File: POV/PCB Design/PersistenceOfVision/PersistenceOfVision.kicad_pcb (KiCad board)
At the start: 2 copper layers, 8 parts, among them SW1 SW_Push, U1 ATtiny85-20PU

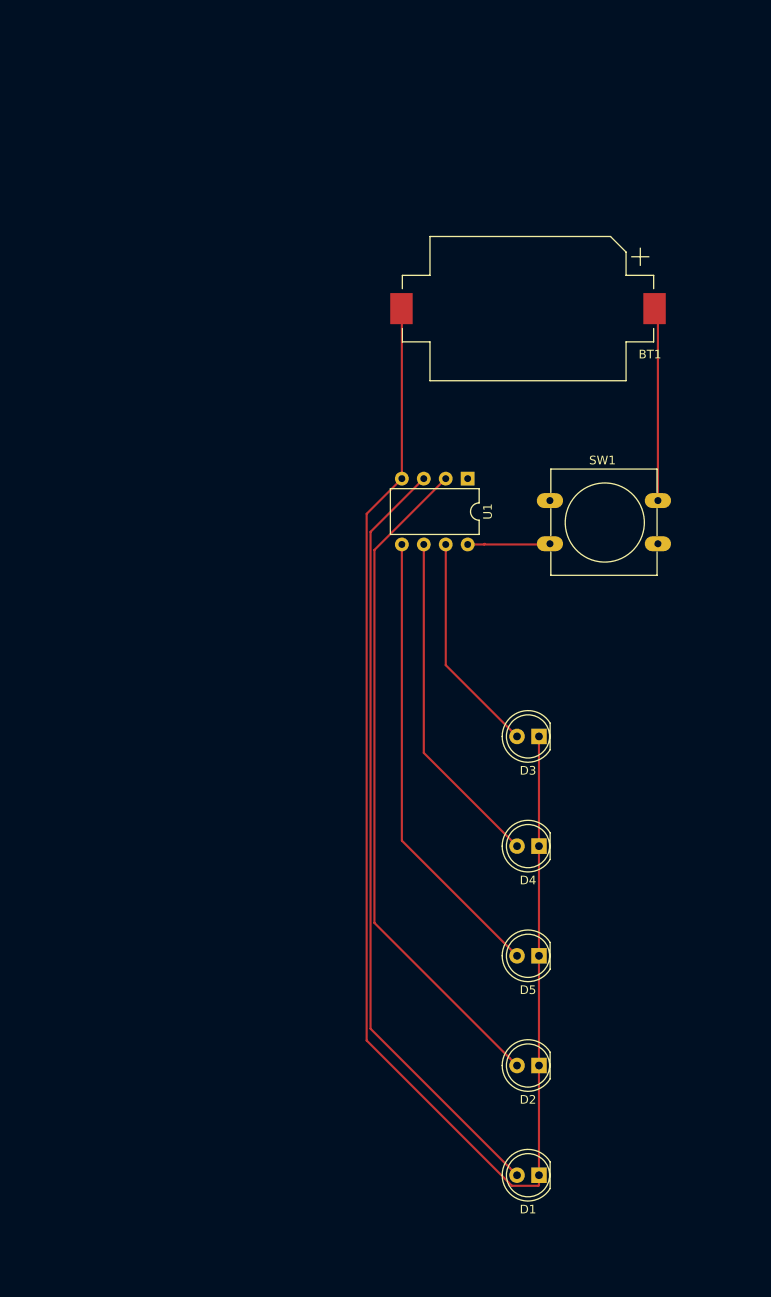
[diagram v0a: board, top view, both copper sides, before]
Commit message: Added graphics to the board
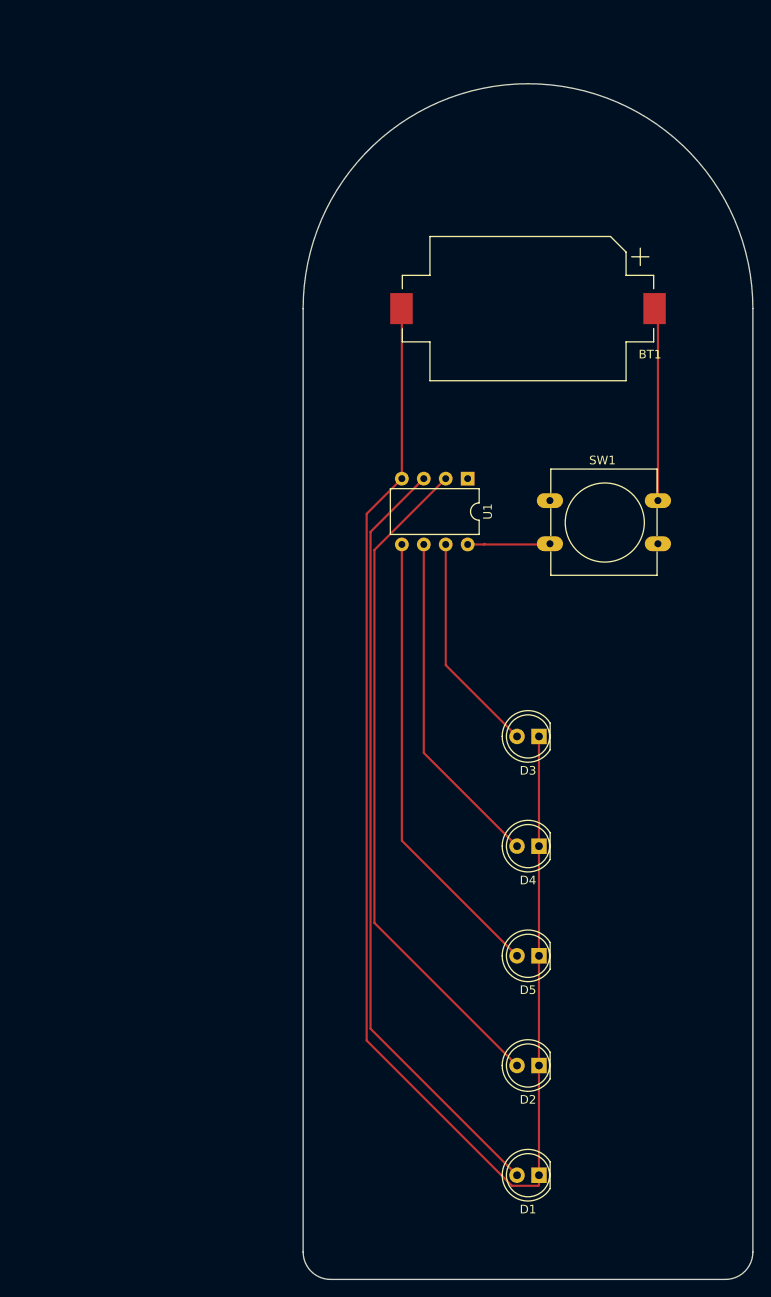
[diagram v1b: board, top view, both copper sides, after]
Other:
- board outline added: 52.1 x 138.4 mm
- board text added: "HaCkEr SPARKIES"
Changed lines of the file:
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@@
   (general
     (thickness 1.6)
-    (drawings 0)
+    (drawings 9)
     (tracks 28)
     (zones 0)
@@
     )
   )
+  (gr_poly (pts (xy 163.83 75.565) (xy 172.72 61.595) (xy 167.64 62.865) (xy 172.72 48.895) (xy 165.735 48.895) (xy 164.465 66.04) (xy 167.64 65.405)) (layer B.SilkS) (width 0.15))
+  (gr_line (start 140.97 62.23) (end 140.97 171.45) (layer Edge.Cuts) (width 0.15))
+  (gr_line (start 193.04 171.45) (end 193.04 62.23) (layer Edge.Cuts) (width 0.15))
+  (gr_line (start 189.865 174.625) (end 189.865 174.625) (layer Edge.Cuts) (width 0.15))
+  (gr_line (start 144.145 174.625) (end 189.865 174.625) (layer Edge.Cuts) (width 0.15))
+  (gr_arc (start 144.145 171.45) (end 140.97 171.45) (angle -90) (layer Edge.Cuts) (width 0.15))
+  (gr_arc (start 189.865 171.45) (end 189.865 174.625) (angle -90) (layer Edge.Cuts) (width 0.15))
+  (gr_text "HaCkEr\n\n\nSPARKIES" (at 167.005 117.475) (layer B.SilkS)
+    (effects (font (size 5 5) (thickness 1.2)) (justify mirror))
+  )
+  (gr_arc (start 167.005 62.23) (end 193.04 62.23) (angle -180) (layer Edge.Cuts) (width 0.15))
   (segment (start 152.4 123.825) (end 165.735 137.16) (width 0.25) (layer F.Cu) (net 2))
   (segment (start 152.4 89.535) (end 152.4 123.825) (width 0.25) (layer F.Cu) (net 2))

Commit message: Updated to new button with wider holes
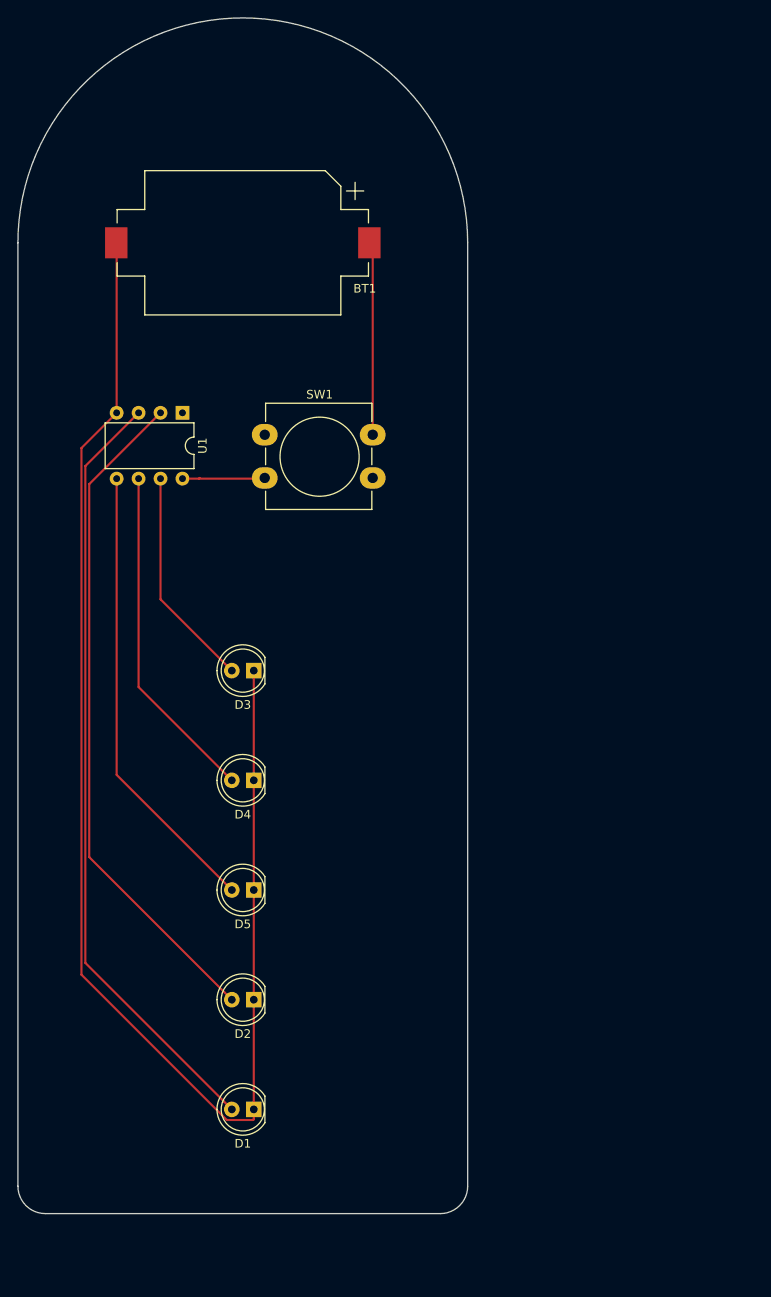
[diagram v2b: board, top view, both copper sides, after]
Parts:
- SW1: footprint Button_Switch_THT:SW_PUSH-12mm -> Button_Switch_THT:SW_PUSH-12mm_Wuerth-430476085716
- moved D1 33.9 mm to (135.3, 154.9)
- moved D2 33.9 mm to (135.3, 142.2)
- moved D3 33.9 mm to (135.3, 104.1)
- moved D5 33.9 mm to (135.3, 129.5)
- moved U1 33.9 mm to (127.0, 74.3)
- moved D4 33.9 mm to (135.3, 116.8)
- moved BT1 33.9 mm to (134.0, 54.6)
- moved SW1 33.9 mm to (136.5, 76.8)
